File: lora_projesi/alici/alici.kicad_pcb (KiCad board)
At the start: 4 copper layers, 88 x 102 mm, 127 parts, among them J1 USB-C, J2 SMA, J3 RJ45, J4 u.FL (ANA ANTEN), J5 12 V GIRIS, J6 LAMBA, J7 MICRO-SIM, J8 u.FL (YARDIMCI ANTEN, ISTEGE 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, K1 SRD-12VDC-SL-A, Q1 AO3401A, Q2 MMBT2222A, Q3 MMBT2222A, Q4 MMBT2222A, SW1 DUGME, U1 ESP32-S3-WROOM-1-N4, U10 SIM7600SA, U11 AP2112K-3.3, U12 ESDA6V1-5SC6, U4 RFM95W-915S2, U5 TPS62933DRLR, U6 TPS62933DRLR, U7 USBLC6-2SC6, U8 TXB0104PW, U9 W5500, Y1 25 MHz

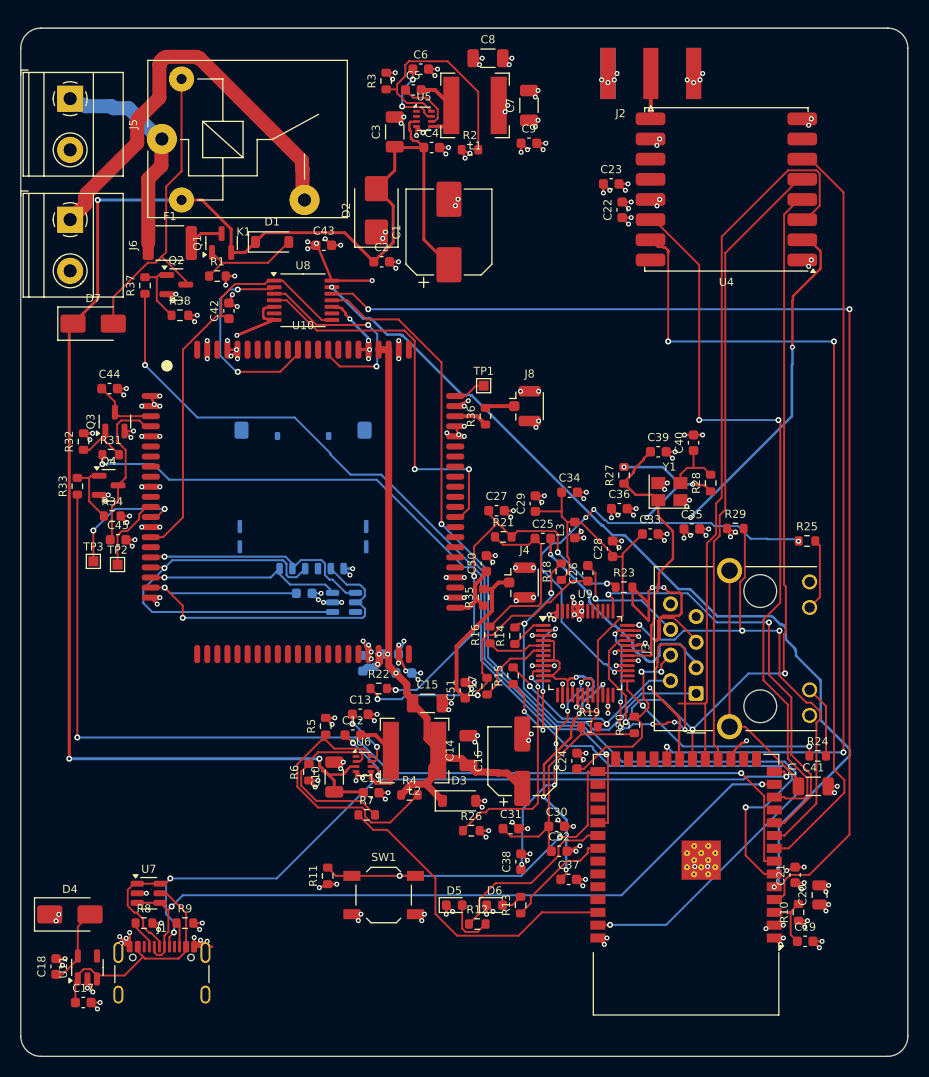
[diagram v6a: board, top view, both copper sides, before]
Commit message: Verici Ra-01H ile yonlendirildi (DRC hata 0); maliyet modeli LCSC fiyatlarina guncellendi; alici yonlendirmesi suruyor
Co-Authored-By: Claude Sonnet 5.5 <noreply@anthropic.com>
Claude-Session: https://claude.ai/code/session_01Q71gHQtKJ86ZE2CtYTYSwP
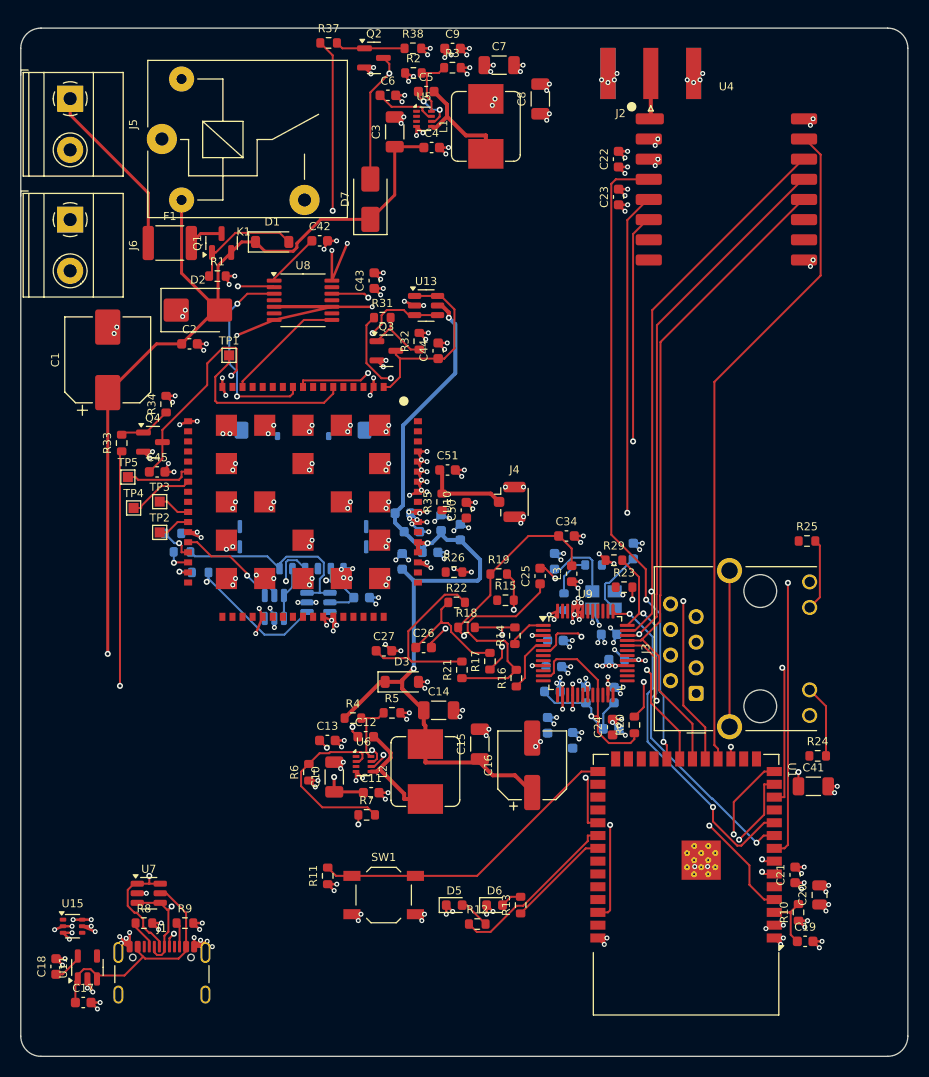
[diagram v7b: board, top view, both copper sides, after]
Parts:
- removed D4: SS14, D_SMA
- removed J8: u.FL (YARDIMCI ANTEN, ISTEGE BAGLI), U.FL_Hirose_U.FL-R-SMT-1_Vertical
- removed R36: 0, R_0603_1608Metric
- added C52: 33pF, C_0603_1608Metric, B.Cu at (37.8, 52.9)
- added C53: 10pF, C_0603_1608Metric, B.Cu at (41.7, 49.1)
- added C54: 1uF, C_0603_1608Metric, B.Cu at (43.6, 50.0)
- added R39: 22, R_0603_1608Metric, B.Cu at (17.8, 54.0)
- added R40: 22, R_0603_1608Metric, B.Cu at (16.0, 52.0)
- added R41: 22, R_0603_1608Metric, B.Cu at (15.1, 50.1)
- added TP4: USB_VBUS, TestPoint_Pad_1.0x1.0mm, F.Cu at (11.2, 47.6)
- added TP5: UART_LOG_TX, TestPoint_Pad_1.0x1.0mm, F.Cu at (10.6, 44.5)
- added U13: USBLC6-2SC6, SOT-23-6, F.Cu at (40.2, 27.5)
- added U14: USBLC6-2SC6, SOT-23-6, B.Cu at (25.2, 57.4)
- added U15: LM66100, SOT-363_SC-70-6, F.Cu at (5.14, 89.1)
- C28, C29, C30, C31, C32, C33, C35, C36, C37, C38, C39, C40, R27, R28, Y1: moved to B.Cu
- C44, C45: value 100nF -> 1nF
- L1, L2: value 4,7uH Isat 2,7A -> 4,7uH Isat 10A; footprint L_Bourns-SRN6028 -> L_Bourns_SRP7028A_7.3x6.6mm
- TP1: value BOOT_CFG0 -> USB_BOOT
- TP2: value USB_DN -> USB_DM
- U10: value SIM7600SA -> A7670SA; footprint SIM7600_LCC87 -> A7670SA_LGA88
- U12: value ESDA6V1-5SC6 -> USBLC6-2SC6
- U4: value RFM95W-915S2 -> Ra-01H; footprint HOPERF_RFM9XW_SMD -> Ra-01H
- moved C1 36.1 mm to (8.63, 32.9)
- moved R38 35.1 mm to (38.9, 2.01)
- moved R32 34.8 mm to (39.5, 31.1)
- moved C44 32.8 mm to (41.4, 32.0), turned to 90 degrees
- moved R37 30.2 mm to (30.5, 1.47), turned to 0 degrees
- moved R31 30.2 mm to (35.9, 28.7)
- moved D7 30.1 mm to (34.7, 17.0), turned to 90 degrees
- moved Q2 29.8 mm to (35.0, 2.96)
- moved Q3 27.8 mm to (36.3, 32.0), turned to 0 degrees
- moved R26 25.7 mm to (43.0, 54.0)
- moved TP1 25.4 mm to (20.7, 32.5)
- moved C51 21.9 mm to (42.3, 43.8), turned to 0 degrees
- moved C2 20.7 mm to (16.7, 31.3)
- moved D2 20.3 mm to (17.6, 28.0), turned to 0 degrees
- moved C33 19.7 mm to (58.6, 69.5)
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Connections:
- TP1 pad 1: BOOT_CFG0 -> USB_BOOT
- U10 pad 1: GND -> PWRKEY
- U10 pad 10: GND -> M_RXD
- U10 pad 12: M_USB_DN -> (no net)
- U10 pad 13: M_USB_DP -> (no net)
- U10 pad 14: GND -> (no net)
- U10 pad 16: (no net) -> MODEM_RESET
- U10 pad 17: USIM_DATA -> GND
- U10 pad 18: USIM_RST -> GND
- U10 pad 19: USIM_CLK -> (no net)
- U10 pad 20: USIM_VDD -> (no net)
- U10 pad 23: (no net) -> LOG_TX
- U10 pad 24: (no net) -> M_USB_VBUS
- U10 pad 27: (no net) -> M_USB_DP
- U10 pad 28: (no net) -> M_USB_DN
- U10 pad 29: (no net) -> GND
- U10 pad 3: PWRKEY -> (no net)
- U10 pad 30: (no net) -> USIM_VDD
- U10 pad 31: (no net) -> USIM_DATA_M
- U10 pad 32: (no net) -> USIM_CLK_M
- U10 pad 33: (no net) -> USIM_RST_M
- U10 pad 37: GND -> (no net)
- U10 pad 38: VBAT_MOD -> (no net)
- U10 pad 39: VBAT_MOD -> GND
- U10 pad 4: MODEM_RESET -> (no net)
- U10 pad 40: GND -> (no net)
- U10 pad 41: GND -> (no net)
- U10 pad 43: GND -> (no net)
- U10 pad 45: (no net) -> GND
- U10 pad 46: (no net) -> GND
- U10 pad 49: M_STATUS -> (no net)
- U10 pad 5: GND -> (no net)
- U10 pad 54: (no net) -> GND
- U10 pad 55: (no net) -> VBAT_MOD
- U10 pad 56: (no net) -> VBAT_MOD
- U10 pad 57: GND -> VBAT_MOD
- U10 pad 59: MODEM_AUX -> GND
- U10 pad 6: (no net) -> USB_BOOT
- U10 pad 60: GND -> MODEM_ANT
- U10 pad 62: VBAT_MOD -> GND
- U10 pad 63: VBAT_MOD -> GND
- U10 pad 66: (no net) -> M_STATUS
- U10 pad 68: M_RXD -> (no net)
- U10 pad 69: (no net) -> GND
- U10 pad 70: (no net) -> GND
- U10 pad 71: M_TXD -> GND
- U10 pad 72: (no net) -> GND
- U10 pad 73: (no net) -> GND
- U10 pad 74: (no net) -> GND
- U10 pad 75: (no net) -> GND
- U10 pad 76: (no net) -> GND
- U10 pad 79: (no net) -> GND
- U10 pad 82: MODEM_ANT -> GND
- U10 pad 83: (no net) -> GND
- U10 pad 84: (no net) -> GND
- U10 pad 85: BOOT_CFG0 -> GND
- U10 pad 86: (no net) -> GND
- U10 pad 87: (no net) -> GND
- U10 pad 9: (no net) -> M_TXD
- U12 pad 4: USIM_DATA -> USIM_CLK
- U12 pad 6: (no net) -> USIM_RST
- U4 pad 1: GND -> ANT_RF
- U4 pad 10: GND -> (no net)
- U4 pad 12: (no net) -> SPI_SCK
- U4 pad 13: +3V3 -> SPI_MISO
- U4 pad 14: LORA_DIO0 -> SPI_MOSI
- U4 pad 15: LORA_DIO1 -> LORA_NSS
- U4 pad 16: (no net) -> GND
- U4 pad 2: SPI_MISO -> GND
- U4 pad 3: SPI_MOSI -> +3V3
- U4 pad 4: SPI_SCK -> LORA_RESET
- U4 pad 5: LORA_NSS -> LORA_DIO0
- U4 pad 6: LORA_RESET -> LORA_DIO1
- U4 pad 8: GND -> (no net)
- U4 pad 9: ANT_RF -> GND
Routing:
- net MODEM_STATUS: track 107.1 -> 0.00 mm, vias 2 -> 0
- net MODEM_RXD_H: track 90.5 -> 0.00 mm, vias 2 -> 0
- net GND: track 237.4 -> 295.4 mm, vias 234 -> 274
- net W_ACTLED: track 44.8 -> 0.00 mm, vias 4 -> 0
- net +12V: track 158.9 -> 118.1 mm, vias 3 -> 2
- net M_STATUS: track 39.3 -> 0.00 mm, vias 2 -> 0
- net SPI_MOSI: track 108.1 -> 74.7 mm, vias 6 -> 2
- net RCT: track 40.3 -> 9.71 mm, vias 2 -> 1
- net MODEM_TXD_H: track 115.1 -> 86.0 mm
- net XO: track 32.0 -> 4.27 mm, vias 4 -> 0
- net MODEM_RESET: track 16.2 -> 43.5 mm, vias 0 -> 2
- net +1V8: track 41.8 -> 17.4 mm
- net TOCAP: track 24.3 -> 0.00 mm, vias 6 -> 0
- net 1V2O: track 24.2 -> 0.00 mm, vias 4 -> 0
- net +3V3A: track 88.5 -> 64.7 mm
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
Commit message: alici: yeni A7670SA karti ana pcb (DRC 0 hata, 0 baglantisiz)
Co-Authored-By: Claude Sonnet 5.5 <noreply@anthropic.com>
Claude-Session: https://claude.ai/code/session_01Q71gHQtKJ86ZE2CtYTYSwP
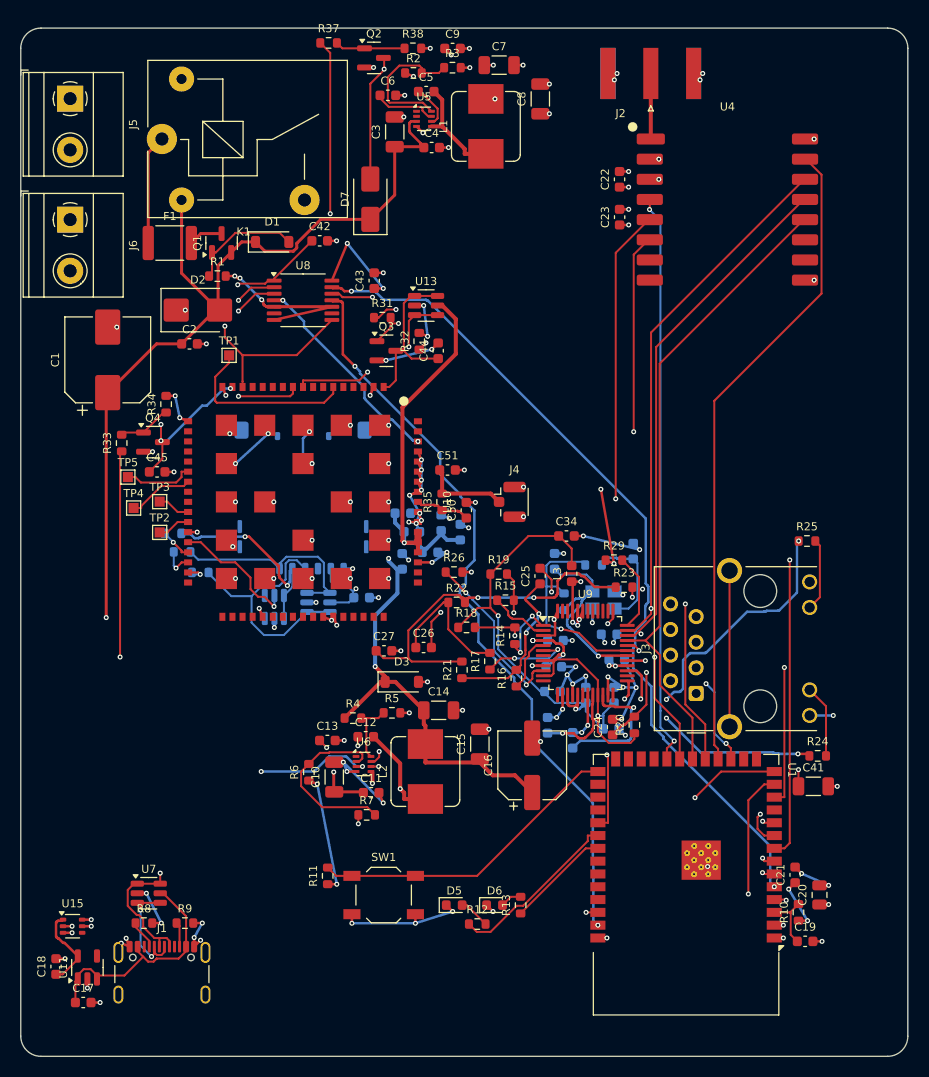
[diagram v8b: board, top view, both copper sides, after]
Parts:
- moved C22 2.00 mm to (59.4, 15.0)
- moved C23 2.00 mm to (59.4, 18.8)
- moved U4 2.00 mm to (70.1, 18.0)
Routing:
- net MODEM_RXD_H: track 0.00 -> 83.7 mm, vias 0 -> 2
- net MODEM_STATUS: track 0.00 -> 74.6 mm, vias 0 -> 2
- net GND: track 295.4 -> 230.4 mm, vias 274 -> 140
- net W_ACTLED: track 0.00 -> 30.7 mm, vias 0 -> 3
- net W_LINKLED: track 0.00 -> 23.2 mm, vias 0 -> 3
- net M_STATUS: track 0.00 -> 21.0 mm, vias 0 -> 2
- net RX_M: track 19.1 -> 37.3 mm, vias 0 -> 2
- net EXRES1: track 0.00 -> 17.1 mm, vias 0 -> 2
- net XO: track 4.27 -> 20.9 mm, vias 0 -> 1
- net USIM_DATA: track 5.29 -> 20.6 mm, vias 0 -> 2
- net ETH_RST: track 34.2 -> 48.8 mm
- net +12V: track 118.1 -> 132.0 mm, vias 2 -> 4
- net +1V8: track 17.4 -> 31.0 mm, vias 0 -> 2
- net 1V2O: track 0.00 -> 13.5 mm, vias 0 -> 1
- net XI: track 7.40 -> 19.5 mm, vias 0 -> 1
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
